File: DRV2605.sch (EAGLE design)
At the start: 107 parts, among them J1 BM06B-SRSS-TB, J2 BM06B-SRSS-TB, J3 BM06B-SRSS-TB, J4 BM06B-SRSS-TB, J5 BM06B-SRSS-TB, J6 JST_6_PIN_VERTICAL, J7 JST_6_PIN_VERTICAL, U1 DRV2605L, U11 NRF51X22_QFQF, U2 DRV2605L, U3 DRV2605L, U4 DRV2605L, U5 DRV2605L, U6 DRV2605L, U7 BNO080, U8 TCA9548APWR, U9 TCA9548APWR, X1 32.768kHz, X2 8MHz, X4 16MHz, X5 32.768kHz, Y1 32.768kHz

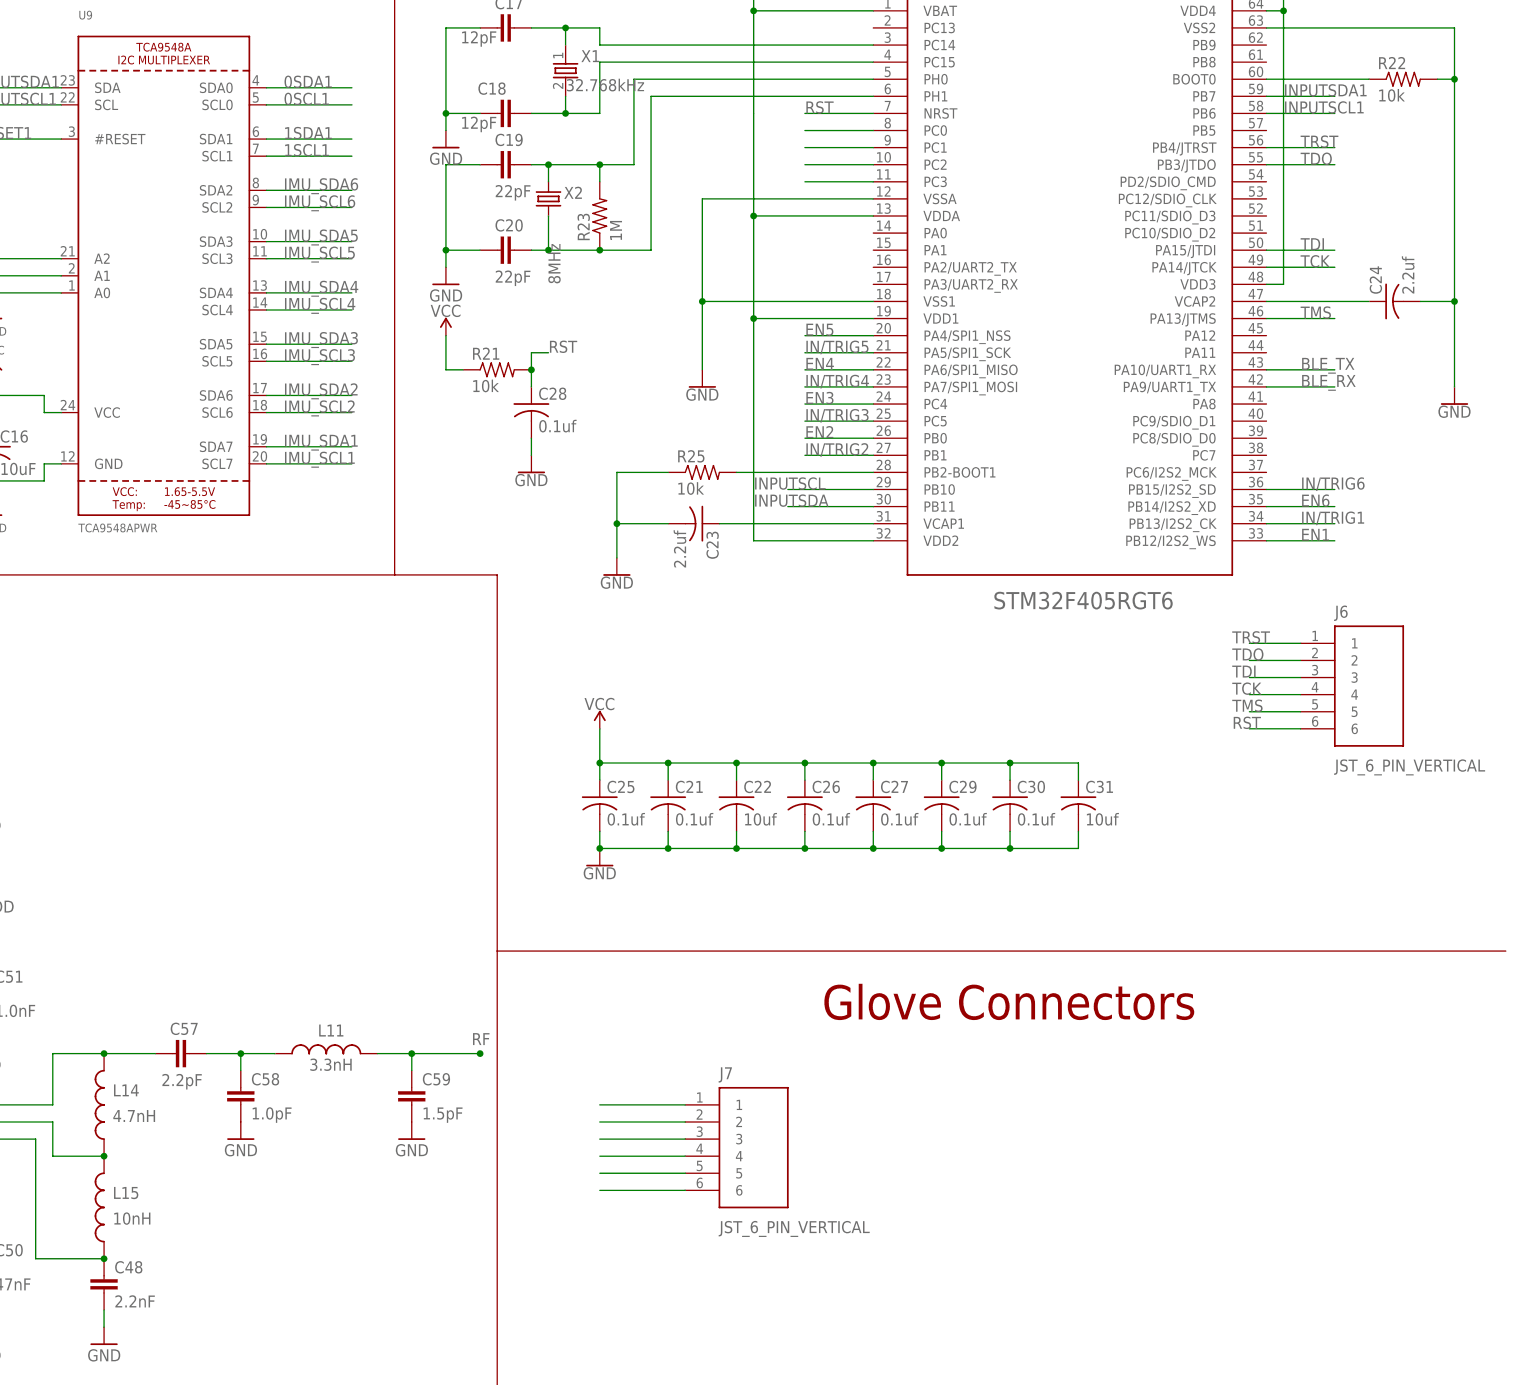
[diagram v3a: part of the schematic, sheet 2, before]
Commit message: NRF antenna yet to be done; glove 50mm wide
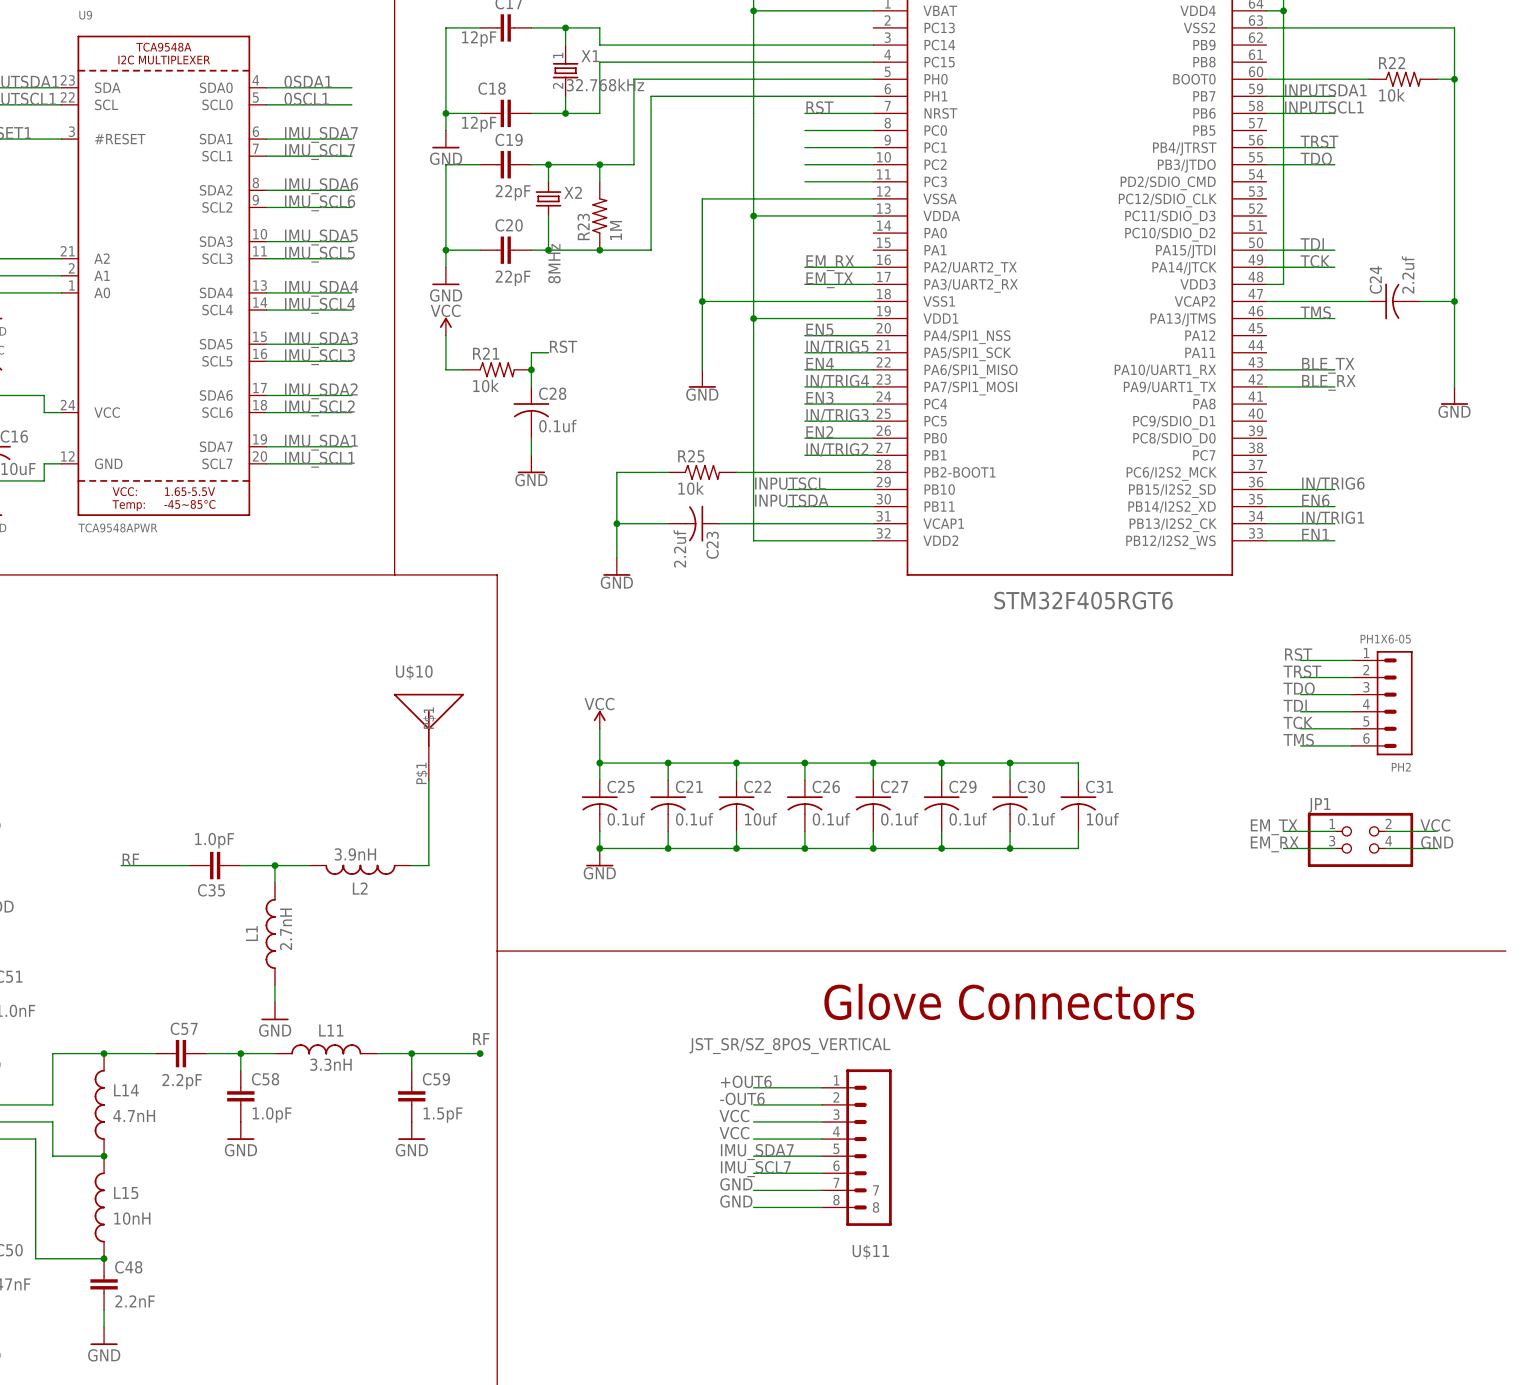
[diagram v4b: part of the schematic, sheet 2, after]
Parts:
- removed J6, J7: JST_6_PIN_VERTICAL, SparkFun-Connectors:JST_6_PIN_VERTICAL
- added C35: 1.0pF, Nordic_nRF:CAPACITOR_0402_N
- added JP1: (no value), pinhead:PINHD-2X2
- added L1: 2.7nH, Nordic_nRF:INDUCTOR_0402_N
- added L2: 3.9nH, Nordic_nRF:INDUCTOR_0402_N
- added PH2: PH1X6-05, pel_hdr:PH1X6-05
- added U$10: ANT_2450AT18B100E, Johanson_antennas:ANT_2450AT18B100E
- added U$11: JST_SR/SZ_8POS_VERTICAL, yhtomit_connectors:JST_SR/SZ_8POS_VERTICAL
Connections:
- removed net 1SCL1: U9.SCL1
- removed net 1SDA1: U9.SDA1
- removed net N$18: J7.3
- removed net N$20: J7.4
- removed net N$21: J7.5
- removed net N$22: J7.6
- new net EM_RX: JP1.3, U$9.PA2/UART2_TX
- new net EM_TX: JP1.1, U$9.PA3/UART2_RX
- new net IMU_SCL7: U$11.6, U9.SCL1
- new net IMU_SDA7: U$11.5, U9.SDA1
- net +OUT6: now also U$11.1
- net -OUT6: now also U$11.2
- net GND: now also JP1.4, L1.1, U$11.7, U$11.8
- net N$15: now also C35.1, L1.2, L2.2; no longer J7.1
- net N$17: now also L2.1, U$10.P$1; no longer J7.2
- net RF: now also C35.2
- net RST: now also PH2.1; no longer J6.6
- net TCK: now also PH2.5; no longer J6.4
- net TDI: now also PH2.4; no longer J6.3
- net TDO: now also PH2.3; no longer J6.2
- net TMS: now also PH2.6; no longer J6.5
- net TRST: now also PH2.2; no longer J6.1
- net VCC: now also JP1.2, U$11.3, U$11.4

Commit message: board done awaiting validation
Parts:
- removed JP1: (no value), pinhead:PINHD-2X2
- removed U$11: JST_SR/SZ_8POS_VERTICAL, yhtomit_connectors:JST_SR/SZ_8POS_VERTICAL
- added C36, C37: 0.1uf, rcl:C-USC0402
- added J6: (no value), SparkFun-Connectors:CONN_04
- added PH1: PH1X4-05, pel_hdr:PH1X4-05
- added U$12: TTP223_SOT23-6, yhtomit_ICs:TTP223_SOT23-6
- added U$13: JST_SR/SZ_9POS_VERTICAL, yhtomit_connectors:JST_SR/SZ_9POS_VERTICAL
- X2: device SparkFun-Clocks:CRYSTALSMD-5X3.2-4PAD -> yhtomit_XTAL:CRYSTAL_5X3.2MM_4PAD
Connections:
- new net IN: C37.1, U$12.IN, U$13.5
- new net N$22: U$12.TOGL
- new net N$24: U$12.AHLB
- new net Q: U$12.Q, U$9.PA12
- net +OUT6: now also U$13.1; no longer U$11.1
- net -OUT6: now also U$13.2; no longer U$11.2
- net EM_RX: now also J6.3; no longer JP1.3
- net EM_TX: now also J6.2; no longer JP1.1
- net GND: now also C36.2, C37.2, J6.4, PH1.1, U$12.VSS, U$13.8, U$13.9, X2.2, X2.4; no longer JP1.4, U$11.7, U$11.8
- net IMU_SCL7: now also U$13.7; no longer U$11.6
- net IMU_SDA7: now also U$13.6; no longer U$11.5
- net PH1: now also X2.3; no longer X2.2
- net SWDCLK: now also PH1.3
- net SWDIO/NRESET: now also PH1.2
- net VCC: now also C36.1, J6.1, PH1.4, U$12.VDD, U$13.3, U$13.4; no longer JP1.2, U$11.3, U$11.4
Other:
- moved on the sheet: C20, C28, R21
